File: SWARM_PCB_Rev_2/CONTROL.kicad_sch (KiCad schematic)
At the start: 51 parts

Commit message: Add MPNs to BOM and apply PCB DFM fixes for JLCPCB
Schematic: added MPN and Manufacturer properties to 205 references
across all sub-sheets (Murata/Yageo/TI/ST/Hirose/JST etc.).
Fixed dU7 description to match INA823DR (not INA828).

PCB: added via tenting (1540 vias), removed stale auto-placement-area
keepout zones (4 zones), increased annular rings on 482 undersized vias
(0.05mm -> 0.1mm), added 6 fiducial markers (3x F.Cu + 3x B.Cu).

Co-Authored-By: Claude Sonnet 4.6 <noreply@anthropic.com>
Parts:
- aC1, aC10, aC11, aC12, aC13, aC2, aC4, aC6, aC7, aC9: MPN (none) -> GRM188R71C104KA01D; Manufacturer (none) -> Murata
- aC14, aC5, aC8: MPN (none) -> GRM188R60J106ME47D; Manufacturer (none) -> Murata
- aC15: MPN (none) -> GRM188R71H103KA01D; Manufacturer (none) -> Murata
- aC16, aC17, aC18, aC19: MPN (none) -> GRM188R61A105KA61D; Manufacturer (none) -> Murata
- aC3: MPN (none) -> GRM188R60J225KE15D; Manufacturer (none) -> Murata
- aFB1: MPN (none) -> BLM18BD121SN1D; Manufacturer (none) -> Murata
- aJ2: MPN (none) -> USB4085-GF-A; Manufacturer (none) -> GCT
- aJ3: MPN (none) -> 1140084168; Manufacturer (none) -> Amphenol
- aR1, aR12, aR2, aR3, aR4: MPN (none) -> RC0603FR-071KL; Manufacturer (none) -> Yageo
- aR10, aR11: MPN (none) -> RC0603FR-074K7L; Manufacturer (none) -> Yageo
- aR13, aR14, aR15, aR16, aR17, aR5, aR6, aR9: MPN (none) -> RC0603FR-0710KL; Manufacturer (none) -> Yageo
- aR7, aR8: MPN (none) -> RC0603FR-075K1L; Manufacturer (none) -> Yageo
- aU1: MPN (none) -> SC0918; Manufacturer (none) -> Raspberry Pi
- aU2: MPN (none) -> STM32F446RET6; Manufacturer (none) -> STMicroelectronics
- aU3: MPN (none) -> USBLC6-2SC6; Manufacturer (none) -> STMicroelectronics
- aY1: MPN (none) -> CM9V-T1A-32.768KDZB-UT; Manufacturer (none) -> MicroCrystal
- aY2: MPN (none) -> FA-238 16.0000MB; Manufacturer (none) -> Seiko Epson

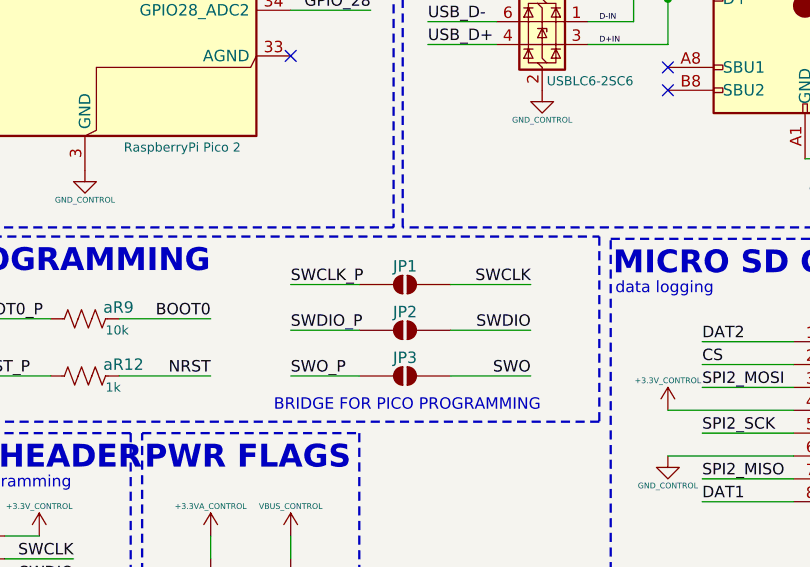
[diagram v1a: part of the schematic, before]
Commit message: Design review fixes: feedback resistor, SWCLK, LED MPNs, GND annotation
- POWER: correct bR10 feedback resistor 187k→255k so TPS55340RTER
  (Vref=0.9V) sets VPiezo to 23.85V (~24V target)
- POWER: assign MPNs for bD2 (green), bD3/bD4 (blue) JE2835 LEDs
- CONTROL: add 33Ω series resistor aR18 on SWCLK near debug header aJ4
- CONTROL: assign MPNs for aD1 (purple) and aD2 (RGB) LEDs
- Top schematic: document isolated GND domain architecture (H3)
- PCB layout, sub-sheet, and SPICE updates

Co-Authored-By: Claude Sonnet 4.6 <noreply@anthropic.com>
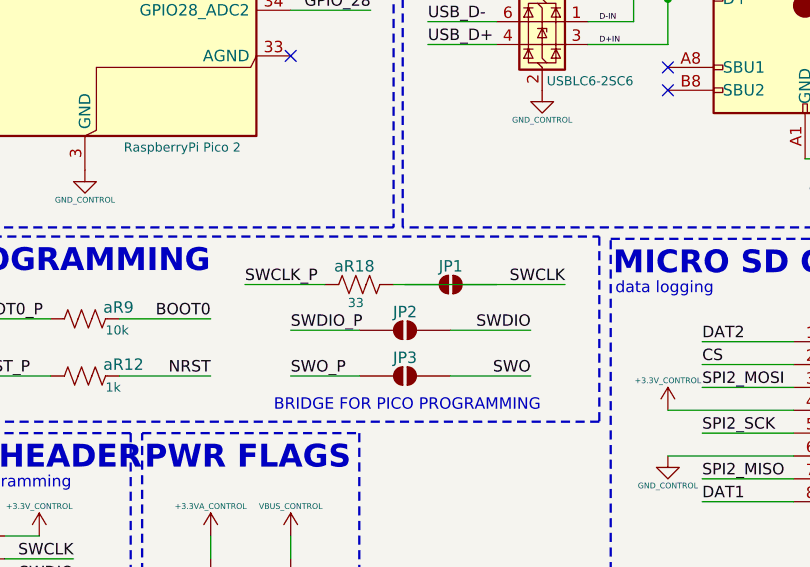
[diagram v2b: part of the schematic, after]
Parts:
- added aR18: 33, Resistor_SMD:R_0603_1608Metric, symbol Device:R_US
- aD1: MP (none) -> JE2835APP-N-0001A0000-N0000001
- aD2: MP (none) -> L1MC-RGB0028000MP0
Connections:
- net SWCLK: now also aR18.1
- net SWCLK_P: now also aR18.2; no longer JP1.1 (A)
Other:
- moved on the sheet: JP1

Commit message: Design review fixes: cap voltage ratings, MPN corrections, FET symbol
- POWER: upgrade 17x MLCC MPNs to correct voltage ratings (6.3V/10V caps
  on 12–24V rails replaced with 25V/50V Murata GRM equivalents)
- POWER: fix bR10 MPN to RC0603FR-07255KL (was 187k part, value is 255k)
- CONTROL: fix aR18 MPN to RC0603FR-0733RL (was 10k part, value is 33R)
- TX_RX: replace IPD50R3K0CE lib symbol with Device:MOSFET_N for dQ1-dQ4
- TX_RX: mark dL1/dL2 value as TBD (piezo matching, pending characterisation)
- DESIGN_REVIEW: full review update with all findings by severity

Co-Authored-By: Claude Sonnet 4.6 <noreply@anthropic.com>
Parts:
- aR18: MPN RC0603FR-0710KL -> RC0603FR-0733RL
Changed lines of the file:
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@@
 			)
 		)
-		(property "MPN" "RC0603FR-0710KL"
+		(property "MPN" "RC0603FR-0733RL"
 			(at 30.48 -3.81 0)
 			(hide yes)

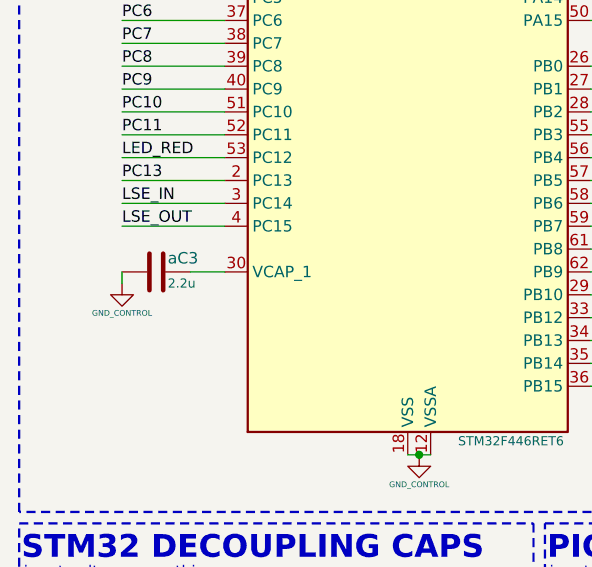
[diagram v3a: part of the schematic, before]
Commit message: Fix VCAP cap value and I2C pull-up resistors
- CONTROL: aC3 VCAP changed 2.2uF -> 1uF (GRM188R60J105KE15D) per STM32F446 spec
- SENSOR: cR1/cR2 I2C pull-ups changed 4.7k -> 2.2k (RC0603FR-072K2L) for 400kHz 4-device bus

Co-Authored-By: Claude Sonnet 4.6 <noreply@anthropic.com>
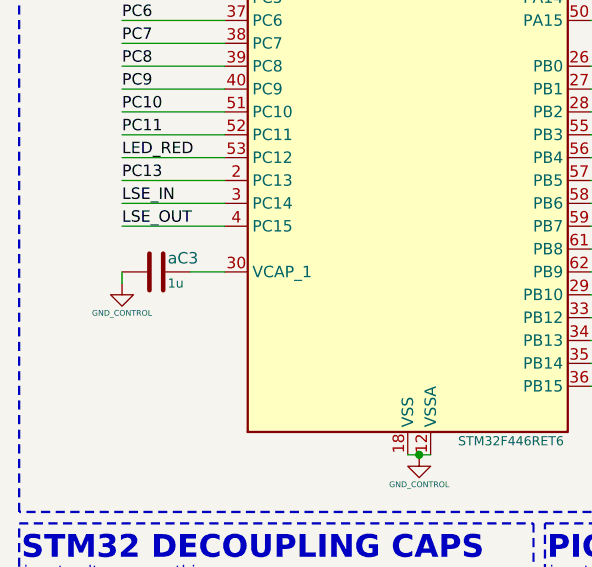
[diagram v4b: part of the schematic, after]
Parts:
- aC3: value 2.2u -> 1u; MPN GRM188R60J225KE15D -> GRM188R60J105KE15D
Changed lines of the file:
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@@
 			)
 		)
-		(property "Value" "2.2u"
+		(property "Value" "1u"
 			(at 29.21 100.33 90)
 			(show_name no)
@@
 			)
 		)
-		(property "MPN" "GRM188R60J225KE15D"
+		(property "MPN" "GRM188R60J105KE15D"
 			(at 0 0 0)
 			(hide yes)
